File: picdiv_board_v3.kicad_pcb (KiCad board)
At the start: 2 copper layers, 75 x 100 mm, 214 parts, among them J1 DC-Input, J101 MountingHole_M2.5, J102 MountingHole_M2.5, J10_PPSB PPS_B, J14 TEST_2P, J2 10MHz-Input, J3 ICSP, J4 SYNC, J5 PPS_A, J6 PPS_B, J7_Fin 10MHz-Input, J8_SYNC SYNC, J9_PPSA PPS_A, Q1 Q_PNP_BEC, Q2 Q_PNP_BEC, SW101 SW_DIP_x03, T1 CM-CHOKE, U1 LT1963A-3.3V, U2 LT1963A, U3 PIC12F675, U4 LTC6993, U5 IDT5PB1108, U6 IDT5PB1108

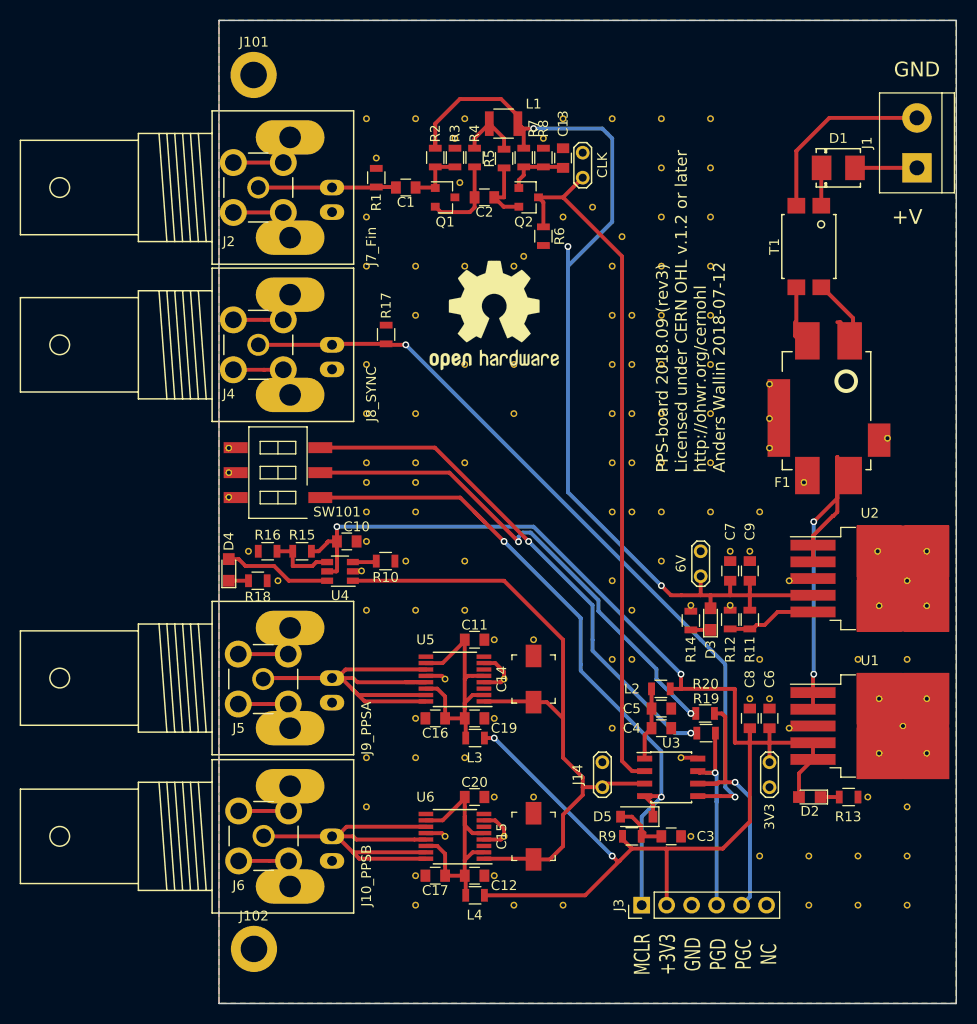
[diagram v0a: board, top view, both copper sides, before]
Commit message: initial layout, symbols to kicad5
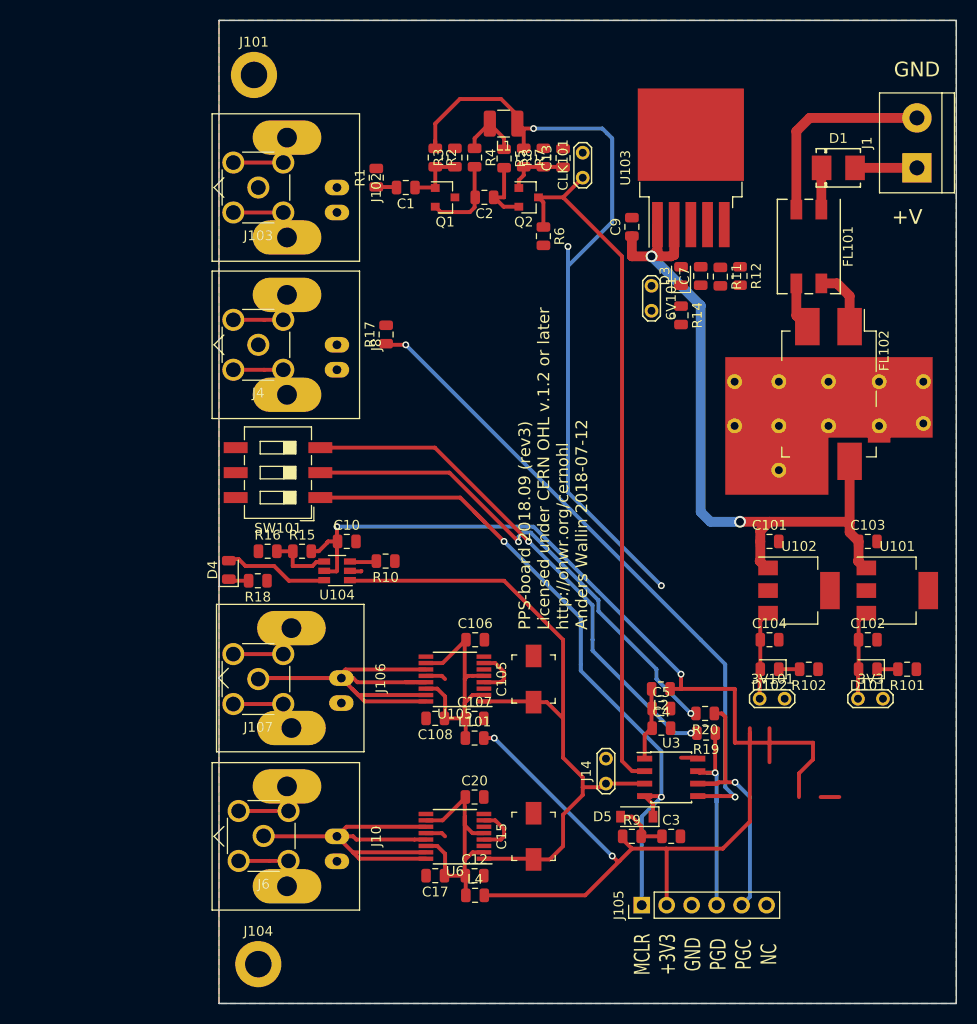
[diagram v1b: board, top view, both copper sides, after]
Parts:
- removed 6V, CLK: TEST_2P, Measurement_Points:Test_Point_2Pads
- removed C11, C16, C19, C6, C8: C, Capacitors_SMD:C_0805
- removed C14: 10p, Capacitors_SMD:C_Trimmer_Murata_TZB4-A
- removed D2: LED, LEDs:LED_0805
- removed F1: BNX025_FILTER, awallinKiCadFootprints:FILTER_BNX025
- removed J10_PPSB: PPS_B, awallinKiCadFootprints:BNC_2PIN
- removed J2: 10MHz-Input, awallinKiCadFootprints:CONNECTOR_SMA_Straight
- removed J3: ICSP, Socket_Strips:Socket_Strip_Straight_1x06_Pitch2.54mm
- removed J5: PPS_A, awallinKiCadFootprints:CONNECTOR_SMA_Straight
- removed J7_Fin: 10MHz-Input, awallinKiCadFootprints:BNC_2PIN
- removed J8_SYNC: SYNC, awallinKiCadFootprints:BNC_2PIN
- removed J9_PPSA: PPS_A, awallinKiCadFootprints:BNC_2PIN
- removed L3: L, Inductors_SMD:L_0805
- removed R13: 82R, Resistors_SMD:R_0805
- removed REF***: OSHW-Logo2_14.6x12mm_SilkScreen, Symbols:OSHW-Logo2_14.6x12mm_SilkScreen
- removed T1: CM-CHOKE, awallinKiCadFootprints:CM-CHOKE
- removed U1: LT1963A-3.3V, TO_SOT_Packages_SMD:TO-263-5_TabPin3
- removed U2: LT1963A, TO_SOT_Packages_SMD:TO-263-5_TabPin3
- removed U4: LTC6993, TO_SOT_Packages_SMD:TSOT-23-6
- removed U5: IDT5PB1108, Housings_SSOP:TSSOP-16_4.4x5mm_Pitch0.65mm
- removed VIA (x138): VIA_0.4mmDrill_0.7mmPad, awallinKiCadFootprints:VIA_0.4mmDrill_0.7mmPad
- added 3V101: TEST_3V3, TestPoint:TestPoint_2Pads_Pitch2.54mm_Drill0.8mm, F.Cu at (180.0, 119.0)
- added 6V101: TEST_6V, TestPoint:TestPoint_2Pads_Pitch2.54mm_Drill0.8mm, F.Cu at (169.0, 77.0)
- added C101: 10u, Capacitor_SMD:C_0805_2012Metric, F.Cu at (181.0, 103.0)
- added C102: 10u, Capacitor_SMD:C_0805_2012Metric, F.Cu at (191.0, 113.0)
- added C103: 10u, Capacitor_SMD:C_0805_2012Metric, F.Cu at (191.0, 103.0)
- added C104: 10u, Capacitor_SMD:C_0805_2012Metric, F.Cu at (181.0, 113.0)
- added C105: 10p, Capacitor_SMD:C_Trimmer_Murata_TZB4-A, F.Cu at (157.0, 117.0)
- added C106: 100n, Capacitor_SMD:C_0805_2012Metric, F.Cu at (151.1, 113.0)
- added C107: 100n, Capacitor_SMD:C_0805_2012Metric, F.Cu at (151.0, 121.0)
- added C108: 100n, Capacitor_SMD:C_0805_2012Metric, F.Cu at (147.0, 121.0)
- added CLK101: TEST_CLK, TestPoint:TestPoint_2Pads_Pitch2.54mm_Drill0.8mm, F.Cu at (162.0, 66.0)
- added D101: LED, LED_SMD:LED_0805_2012Metric, F.Cu at (191.0, 116.0)
- added D102: LED, LED_SMD:LED_0805_2012Metric, F.Cu at (181.0, 116.0)
- added FL101: EMI_Filter_LL_1423, awallinKiCadFootprints:Filter_Bourns_SRF0905_6.0x9.2mm, F.Cu at (185.0, 73.0)
- added FL102: BNX025, Filter:Filter_Murata_BNX025_ThermalVias, F.Cu at (187.0, 88.0)
- added J10: PPS_B, Connector_Coaxial:BNC_Amphenol_B6252HB-NPP3G-50_Horizontal, F.Cu at (137.0, 133.0)
- added J103: Conn_Coaxial, Connector_Coaxial:SMA_Molex_73251-2200_Horizontal, F.Cu at (129.0, 67.0)
- added J104: MountingHole_M2.5, MountingHole:MountingHole_2.7mm_M2.5_DIN965_Pad, F.Cu at (129.0, 146.0)
- added J105: Conn_01x06, Connector_PinHeader_2.54mm:PinHeader_1x06_P2.54mm_Vertical, F.Cu at (168.0, 140.0)
- added J106: PPS_A, Connector_Coaxial:BNC_Amphenol_B6252HB-NPP3G-50_Horizontal, F.Cu at (137.4, 116.9)
- added J107: PPS_A, Connector_Coaxial:SMA_Molex_73251-2200_Horizontal, F.Cu at (129.0, 117.0)
- added J8: SYNC, Connector_Coaxial:BNC_Amphenol_B6252HB-NPP3G-50_Horizontal, F.Cu at (137.0, 83.0)
- added L101: 2u2, Inductor_SMD:L_0805_2012Metric, F.Cu at (151.0, 123.0)
- added R101: 82R, Resistor_SMD:R_0805_2012Metric, F.Cu at (195.0, 116.0)
- added R102: 82R, Resistor_SMD:R_0805_2012Metric, F.Cu at (185.0, 116.0)
- added U101: LT1963AxT-3.3, Package_TO_SOT_SMD:SOT-223-3_TabPin2, F.Cu at (194.0, 108.0)
- added U102: LT1963AxT-3.3, Package_TO_SOT_SMD:SOT-223-3_TabPin2, F.Cu at (184.0, 108.0)
- added U103: LT1963AEQ, Package_TO_SOT_SMD:TO-263-5_TabPin3, F.Cu at (173.0, 65.0)
- added U104: LTC6993xS6-1, Package_TO_SOT_SMD:TSOT-23-6, F.Cu at (137.0, 106.0)
- added U105: IDT5PB1108, Package_SO:TSSOP-16_4.4x5mm_P0.65mm, F.Cu at (149.0, 117.0)
- 3V3: value TEST_2P -> TEST_3V3; footprint Measurement_Points:Test_Point_2Pads -> TestPoint:TestPoint_2Pads_Pitch2.54mm_Drill0.8mm
- C1, C10, C13, C2, C3: footprint Capacitors_SMD:C_0805 -> Capacitor_SMD:C_0805_2012Metric
- C12, C17, C20, C4: value C -> 100n; footprint Capacitors_SMD:C_0805 -> Capacitor_SMD:C_0805_2012Metric
- C15: footprint Capacitors_SMD:C_Trimmer_Murata_TZB4-A -> Capacitor_SMD:C_Trimmer_Murata_TZB4-A
- C5, C7, C9: value C -> 10u; footprint Capacitors_SMD:C_0805 -> Capacitor_SMD:C_0805_2012Metric
- D3, D4: footprint LEDs:LED_0805 -> LED_SMD:LED_0805_2012Metric
- J101: footprint Mounting_Holes:MountingHole_2.7mm_M2.5_DIN965_Pad -> MountingHole:MountingHole_2.7mm_M2.5_DIN965_Pad
- J102: value MountingHole_M2.5 -> Conn_Coaxial; footprint Mounting_Holes:MountingHole_2.7mm_M2.5_DIN965_Pad -> Connector_Coaxial:BNC_Amphenol_B6252HB-NPP3G-50_Horizontal
- J14: value TEST_2P -> TEST_1PPS; footprint Measurement_Points:Test_Point_2Pads -> TestPoint:TestPoint_2Pads_Pitch2.54mm_Drill0.8mm
- J4, J6: footprint awallinKiCadFootprints:CONNECTOR_SMA_Straight -> Connector_Coaxial:SMA_Molex_73251-2200_Horizontal
- L1: footprint Inductors_SMD:L_1210 -> Inductor_SMD:L_1210_3225Metric
- L2, L4: value L -> 2u2; footprint Inductors_SMD:L_0805 -> Inductor_SMD:L_0805_2012Metric
- R1: value 50R -> 49R9; footprint Resistors_SMD:R_0805 -> Resistor_SMD:R_0805_2012Metric
- R10, R11, R12, R14, R15, R16, R17, R18, R19, R2, R20, R3, R4, R5, R6, R7, R8, R9: footprint Resistors_SMD:R_0805 -> Resistor_SMD:R_0805_2012Metric
- SW101: footprint Buttons_Switches_SMD:SW_DIP_x3_W8.61mm_Slide_LowProfile -> Button_Switch_SMD:SW_DIP_SPSTx03_Slide_6.7x9.18mm_W8.61mm_P2.54mm_LowProfile
- U3: footprint Housings_SOIC:SOIC-8_3.9x4.9mm_Pitch1.27mm -> Package_SO:SOIC-8_3.9x4.9mm_P1.27mm
- U6: footprint Housings_SSOP:TSSOP-16_4.4x5mm_Pitch0.65mm -> Package_SO:TSSOP-16_4.4x5mm_P0.65mm
- moved J102 77.9 mm to (137.0, 67.0), turned to 90 degrees
- moved C9 37.0 mm to (167.0, 71.0)
- moved D3 35.0 mm to (172.0, 76.0)
- moved R11 35.0 mm to (176.0, 76.1)
- moved R12 35.0 mm to (178.0, 76.0), turned to 270 degrees
- moved R14 31.1 mm to (172.0, 80.0), turned to 270 degrees
- moved C7 30.1 mm to (174.0, 76.0), turned to 90 degrees
- moved 3V3 11.1 mm to (190.0, 119.0), turned to 0 degrees
- moved J14 2.21 mm to (164.4, 127.6), turned to 90 degrees
- turned J4 to 90 degrees
- turned J6 to 90 degrees
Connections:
- net Net-(C12-Pad1) renamed /U6_3V3
- net Net-(D1-Pad2) renamed /w1
- net Net-(J10-Pad1) renamed /PPS_B
- net Net-(J4-Pad1) renamed /sync
- net Net-(R19-Pad2) renamed /B
- net Net-(R20-Pad2) renamed /A
- 3V3 pad 1: +3V3 -> 3V3_PIC
- C10 pad 1: +3V3 -> 3V3_OUT
- C9 pad 1: +6V -> LDO_IN
- D1 pad 1: Net-(D1-Pad1) -> /w2
- J1 pad 2: Net-(J1-Pad2) -> /w4
- J102 pad 1: GND -> Net-(C1-Pad2)
- J14 pad 1: GND -> PPS
- J14 pad 2: PPS -> GND
- L2 pad 1: +3V3 -> Net-(C4-Pad1)
- L2 pad 2: Net-(C4-Pad1) -> 3V3_PIC
- L4 pad 2: +3V3 -> 3V3_OUT
- R15 pad 2: +3V3 -> 3V3_OUT
- R9 pad 1: +3V3 -> 3V3_PIC
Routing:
- net LDO_IN: track 0.00 -> 73.9 mm, vias 0 -> 2
- net Net-(J5-Pad1): track 52.8 -> 0.00 mm
- net /PPS_A: track 0.00 -> 52.8 mm
- net Net-(F1-PadCB): track 38.4 -> 0.00 mm, vias 2 -> 0
- net /U6_3V3: track 27.0 -> 53.5 mm
- net Net-(C11-Pad1): track 26.5 -> 0.00 mm
- net +6V: track 104.2 -> 80.6 mm
- net /w4: track 0.00 -> 20.8 mm
- net Net-(J1-Pad2): track 19.2 -> 0.00 mm
- net /sync: track 79.1 -> 66.1 mm
- net Net-(C1-Pad2): track 14.0 -> 2.09 mm
- net Net-(R11-Pad2): track 9.14 -> 0.00 mm
- net 3V3_PIC: track 0.00 -> 9.05 mm
- net 3V3_OUT: track 0.00 -> 9.05 mm
- net Net-(F1-PadB): track 8.38 -> 0.00 mm
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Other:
- net class wide added: clearance 0.2, trace_width 1, via_dia 1.2, via_drill 0.8
- board text added: "100mm vertically into 3U rack-box. for horizontal mounting into 1U box, consider 99mm wide PCB, to mount 4pcs side-by-side at 100mm intervals?"
- board text removed: "for horizontal mounting into 1U box, (consider 99mm wide PCB, to mount 4pcs side-by-side at 100mm intervals?)"

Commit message: pcb passes DRC
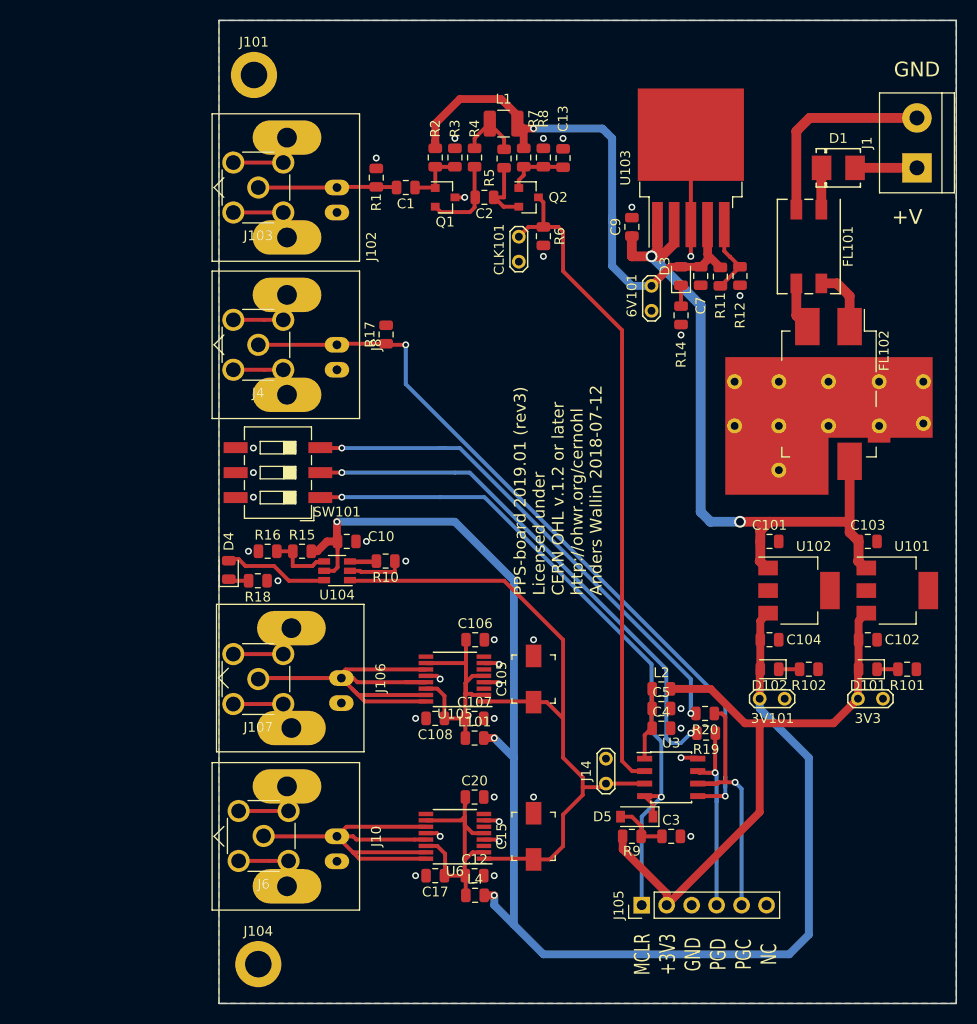
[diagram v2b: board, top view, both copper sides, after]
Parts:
- moved CLK101 8.85 mm to (155.5, 72.0), turned to 270 degrees
- moved L2 0.05 mm to (170.0, 118.0), turned to 0 degrees
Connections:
- C106 pad 1: /U6_3V3 -> /U105_3V3
- C107 pad 1: /U6_3V3 -> /U105_3V3
- C108 pad 1: /U6_3V3 -> /U105_3V3
- L101 pad 1: /U6_3V3 -> /U105_3V3
- SW101 pad 2: /A -> /B
- SW101 pad 3: /B -> /A
- U105 pad 10: /U6_3V3 -> /U105_3V3
- U105 pad 14: /U6_3V3 -> /U105_3V3
- U105 pad 2: /U6_3V3 -> /U105_3V3
- U105 pad 5: /U6_3V3 -> /U105_3V3
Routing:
- net +3V3: track 147.8 -> 0.00 mm, vias 4 -> 0
- net 3V3_OUT: track 9.05 -> 140.7 mm, vias 0 -> 3
- net 3V3_PIC: track 9.05 -> 61.9 mm
- net /U6_3V3: track 53.5 -> 26.7 mm
- net /U105_3V3: track 0.00 -> 26.0 mm
- net +6V: track 80.6 -> 60.8 mm, vias 3 -> 1
- net GND: track 63.4 -> 76.4 mm, vias 0 -> 35
- net /sync: track 66.1 -> 78.6 mm
- net Net-(C1-Pad2): track 2.09 -> 14.1 mm
- net Net-(R11-Pad2): track 0.00 -> 7.76 mm
- net /A: track 50.6 -> 54.4 mm
- net CLK: track 71.1 -> 67.4 mm
- net Net-(R10-Pad2): track 2.42 -> 5.13 mm
- net Net-(D3-Pad1): track 0.00 -> 2.12 mm
- net Net-(D2-Pad1): track 1.90 -> 0.00 mm
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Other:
- board text added: "PPS-board 2019.01 (rev3) Licensed under CERN OHL v.1.2 or later http://ohwr.org/cernohl Anders Wallin 2018-07-12"
- board text removed: "PPS-board 2018.09 (rev3) Licensed under CERN OHL v.1.2 or later http://ohwr.org/cernohl Anders Wallin 2018-07-12"

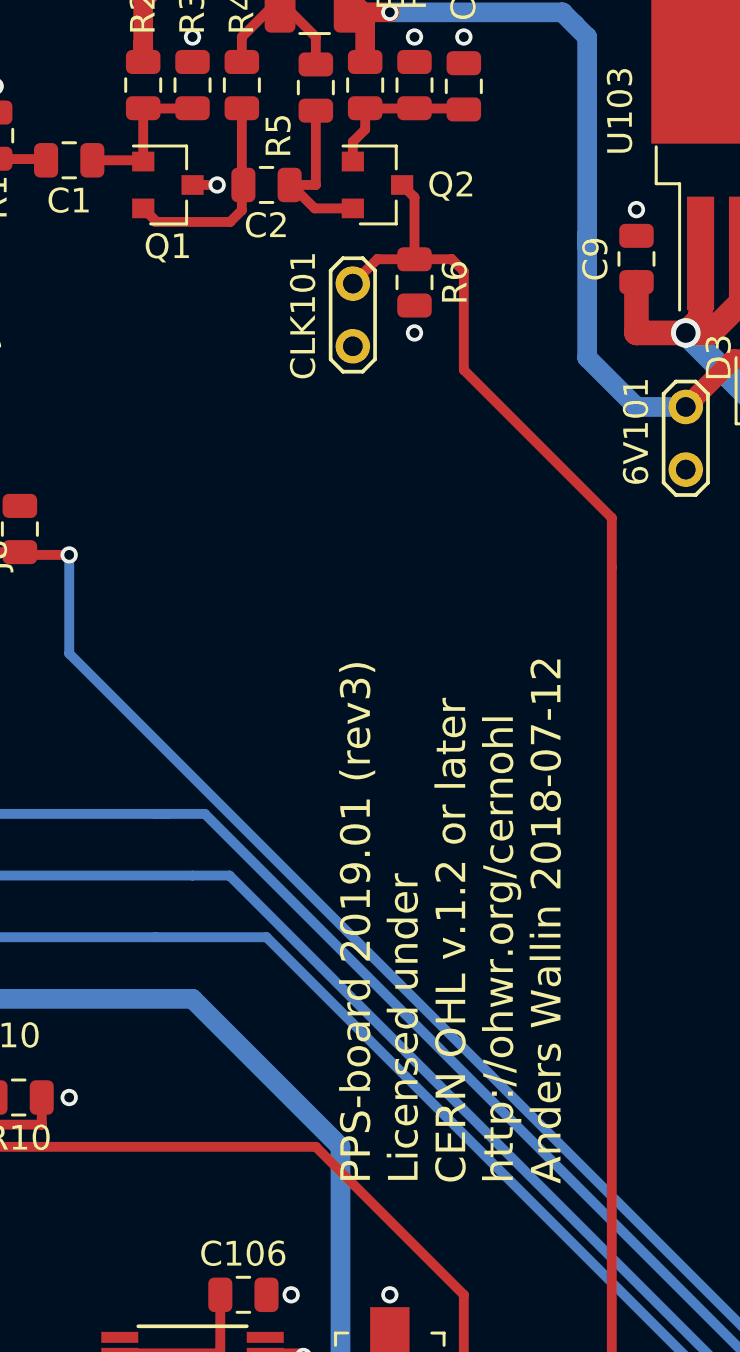
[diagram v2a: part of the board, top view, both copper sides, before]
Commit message: add URL to silk
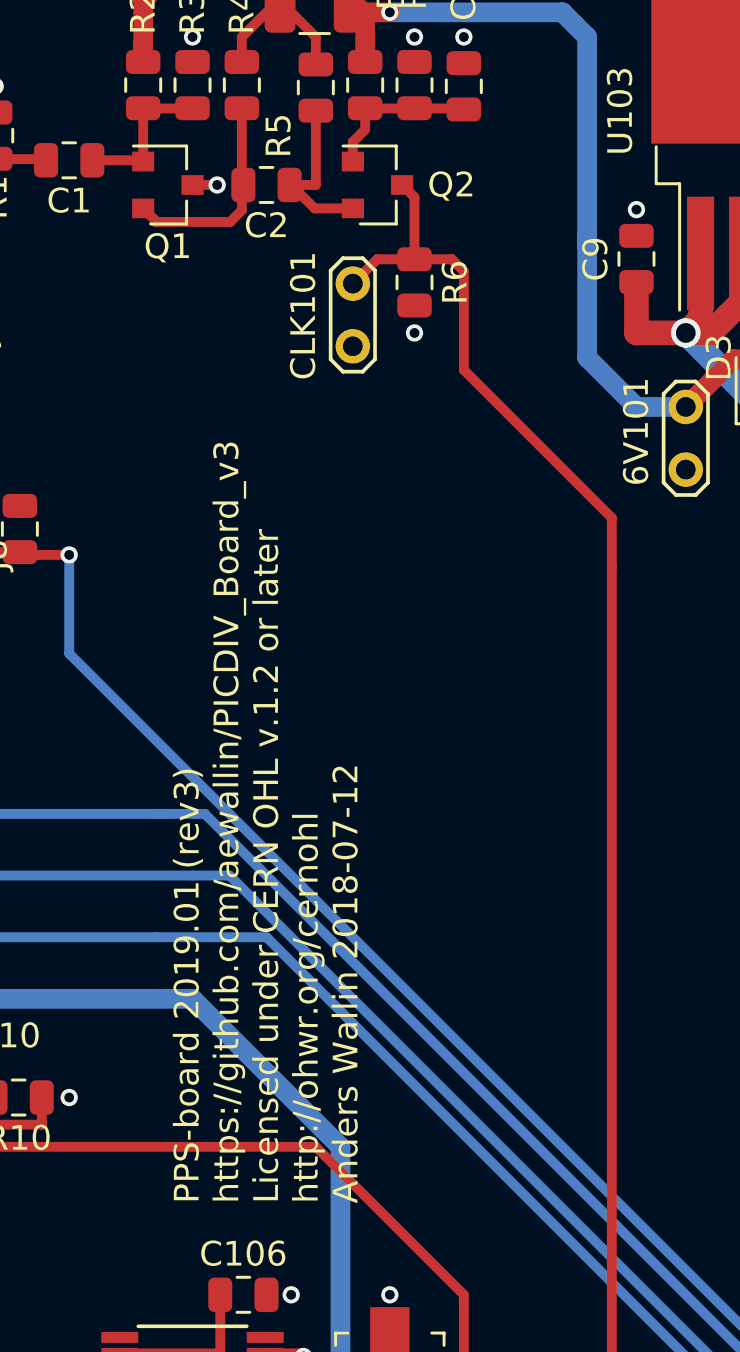
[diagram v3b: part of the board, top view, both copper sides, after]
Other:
- board text added: "PPS-board 2019.01 (rev3) https://github.com/aewallin/PICDIV_Board_v3 Licensed under CERN OHL v.1.2 or later http://ohwr.org/cernohl Anders Wallin 2018-07-12"
- board text removed: "PPS-board 2019.01 (rev3) Licensed under CERN OHL v.1.2 or later http://ohwr.org/cernohl Anders Wallin 2018-07-12"
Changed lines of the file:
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@@
-(kicad_pcb (version 20171130) (host pcbnew 5.0.2-bee76a0~70~ubuntu18.04.1)
+(kicad_pcb (version 20171130) (host pcbnew 5.1.0-060a0da~80~ubuntu18.04.1)
   (general
     (thickness 1.6)
@@
     (zone_45_only no)
     (trace_min 0.2)
-    (segment_width 0.2)
-    (edge_width 0.15)
     (via_size 0.7)
     (via_drill 0.4)
@@
     (uvia_min_size 0.2)
     (uvia_min_drill 0.1)
+    (edge_width 0.15)
+    (segment_width 0.2)
     (pcb_text_width 0.3)
     (pcb_text_size 1.5 1.5)
@@
     (effects (font (size 1.6 1.1) (thickness 0.25)))
   )
-  (gr_text "PPS-board 2019.01 (rev3)\nLicensed under \nCERN OHL v.1.2 or later\nhttp://ohwr.org/cernohl\nAnders Wallin 2018-07-12" (at 159.5 108.5 90) (layer F.SilkS)
-    (effects (font (size 1.2 1.2) (thickness 0.3)) (justify left))
+  (gr_text "PPS-board 2019.01 (rev3)\nhttps://github.com/aewallin/PICDIV_Board_v3\nLicensed under CERN OHL v.1.2 or later\nhttp://ohwr.org/cernohl\nAnders Wallin 2018-07-12" (at 152 109.3 90) (layer F.SilkS)
+    (effects (font (size 1 1) (thickness 0.25)) (justify left))
   )
   (gr_text GND (at 196 55) (layer F.SilkS)
